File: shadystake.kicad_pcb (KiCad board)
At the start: 2 copper layers, 96.8 x 181.5 mm, 40 parts, among them J1 6P6C, J2 6P6C, J3 6P6C, J4 6P6C, J5 6P6C, J6 6P6C, J7 8P8C

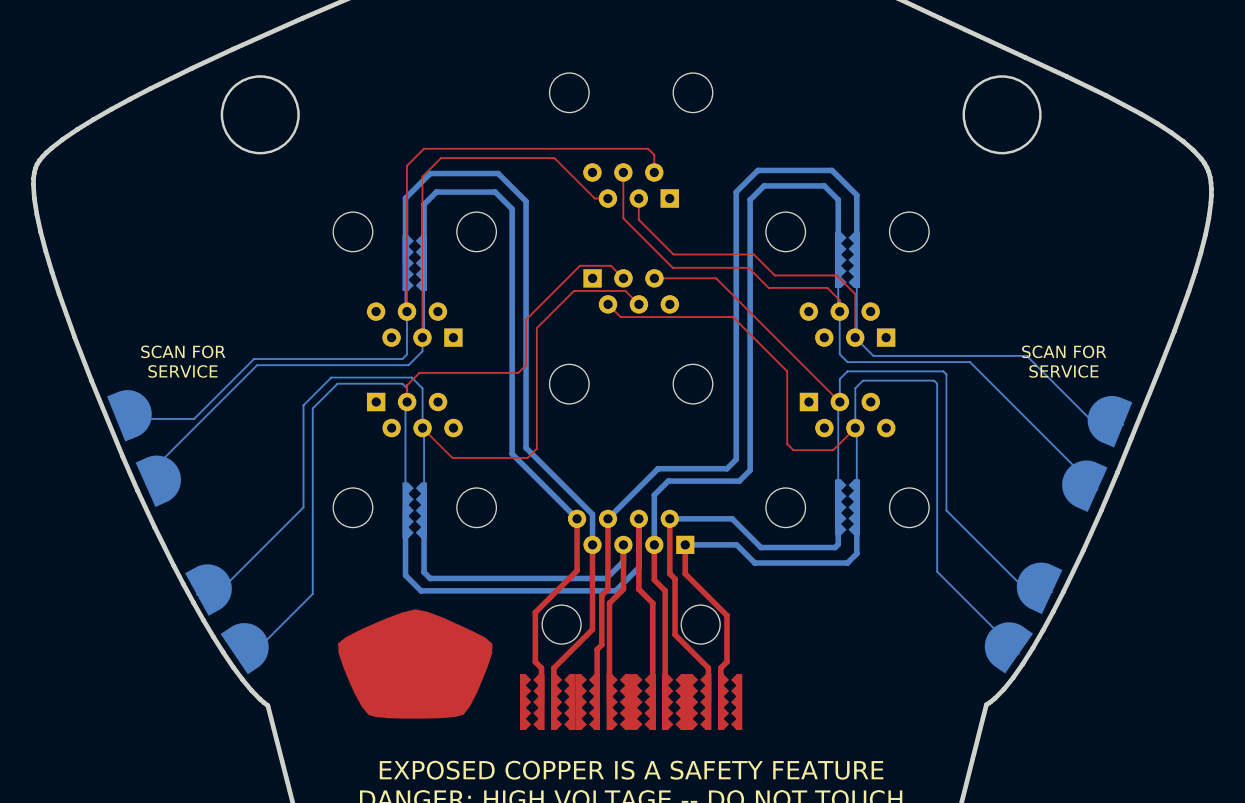
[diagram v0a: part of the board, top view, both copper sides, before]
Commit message: Update to KiCAD 10 and remove circuit protection
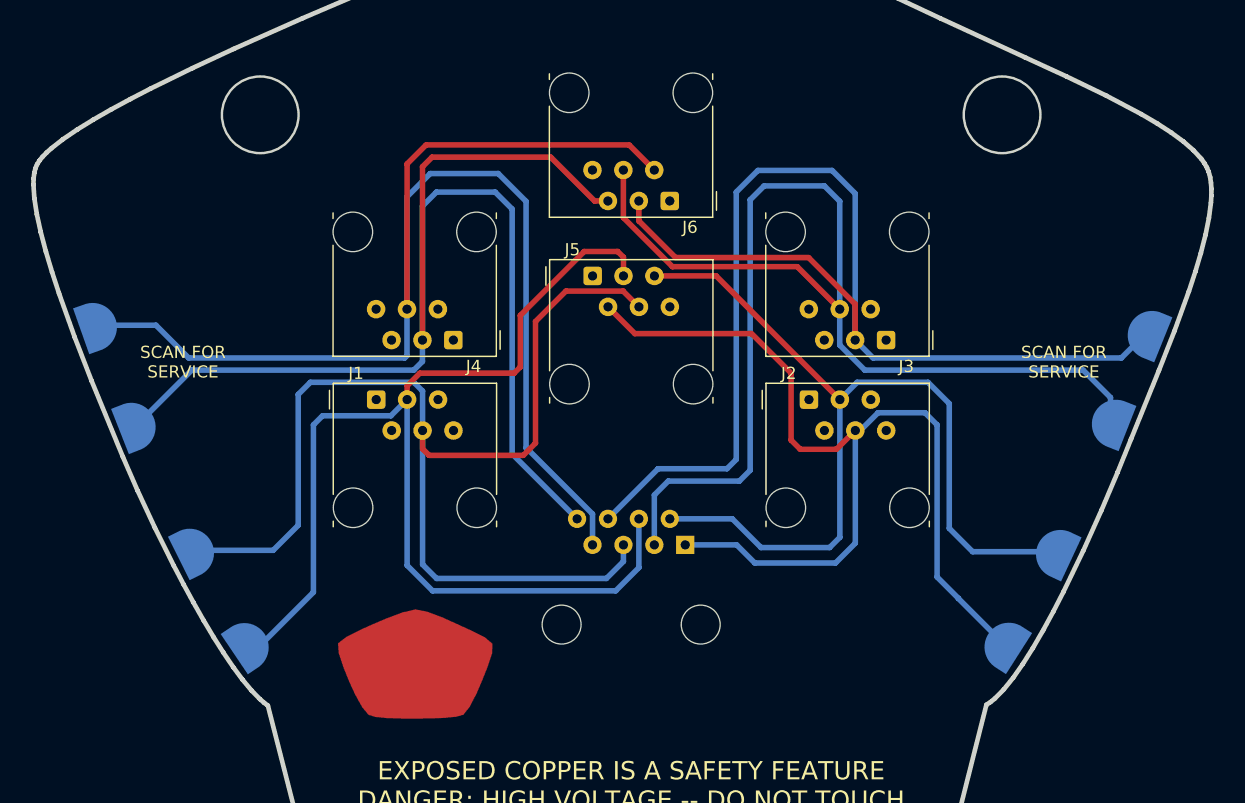
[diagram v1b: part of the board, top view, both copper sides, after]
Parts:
- removed E1, E10, E11, E12, E2, E3, E4, E5, E6, E7, E8, E9: SPARK_GAP, Shadystake:Spark_Gap_Teeth
- J1, J2, J3, J4, J5, J6: footprint Shadystake:6P4C_Vert -> Connector_RJ:RJ12_Amphenol_54601-x06_Horizontal
- moved TP7 7.76 mm to (41.2, 50.8), turned to -160.5 degrees
- moved TP6 7.72 mm to (130.1, 51.5)
- moved TP5 5.60 mm to (127.1, 58.8), turned to -21.5 degrees
- moved TP8 4.85 mm to (44.4, 59.0), turned to -158.5 degrees
- moved TP1 3.31 mm to (49.2, 69.5), turned to -153.5 degrees
- moved TP4 3.11 mm to (122.5, 69.6)
- moved svg2mod 0.20 mm to (43.9, 38.6)
- turned TP3 to -32.5 degrees
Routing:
- net /TIP2: track 104.8 -> 81.7 mm
- net /RING2: track 96.2 -> 76.3 mm
- net /RING1: track 112.3 -> 95.6 mm
- net /RING3: track 123.8 -> 108.6 mm
- net /RING4: track 122.2 -> 107.3 mm
- net /TIP4: track 128.8 -> 115.6 mm
- net /TIP1: track 109.0 -> 95.8 mm
- net /TIP3: track 120.3 -> 109.4 mm

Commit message: Update QR code?
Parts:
- J1, J2, J3, J4, J5, J6: footprint Connector_RJ:RJ12_Amphenol_54601-x06_Horizontal -> Shadystake:RJ12_Amphenol_54601-x06_Horizontal
- svg2mod (x2): footprint Shadystake:fap -> Shadystake:Steak_QR
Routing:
- net /TIP3: track 109.4 -> 108.2 mm

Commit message: Reimport edge.cuts... jfc...
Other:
- outline, holes or cut-outs redrawn

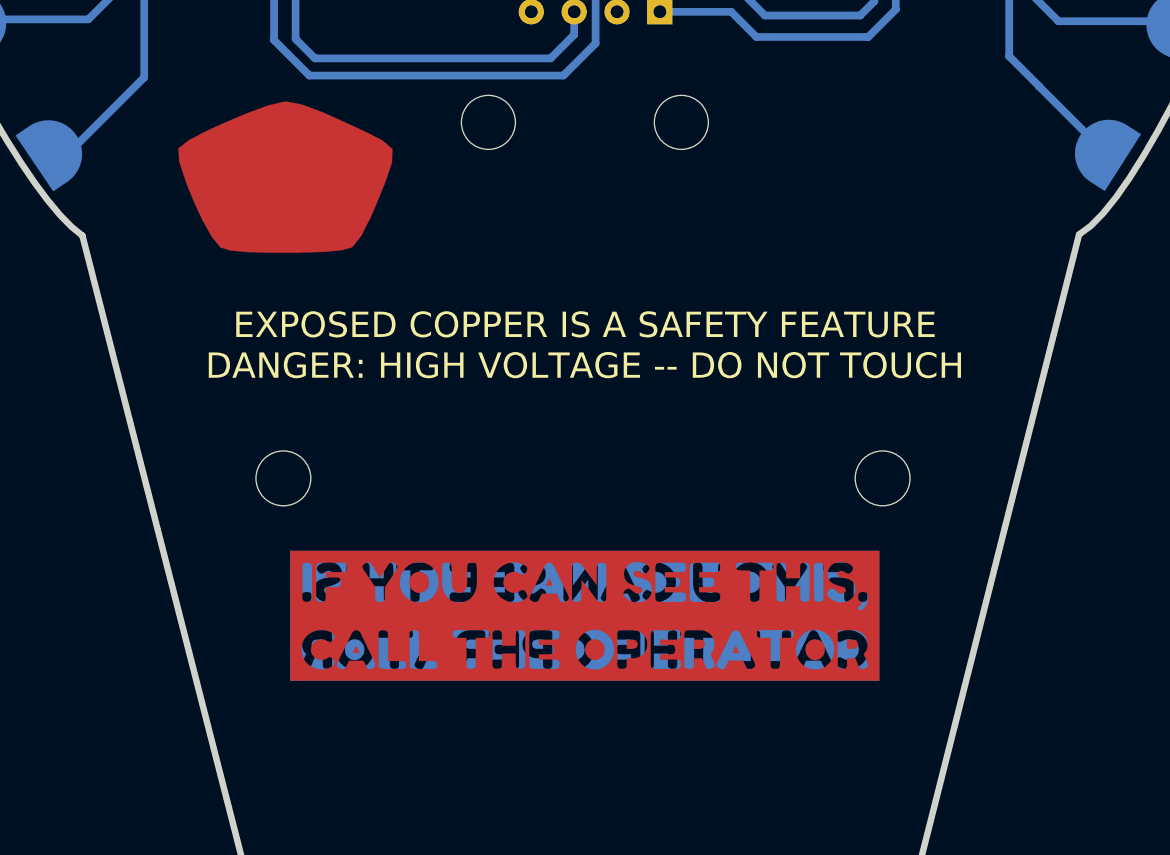
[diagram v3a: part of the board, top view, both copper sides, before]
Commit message: Add silkscreen barcode area and RJ45 eject hole
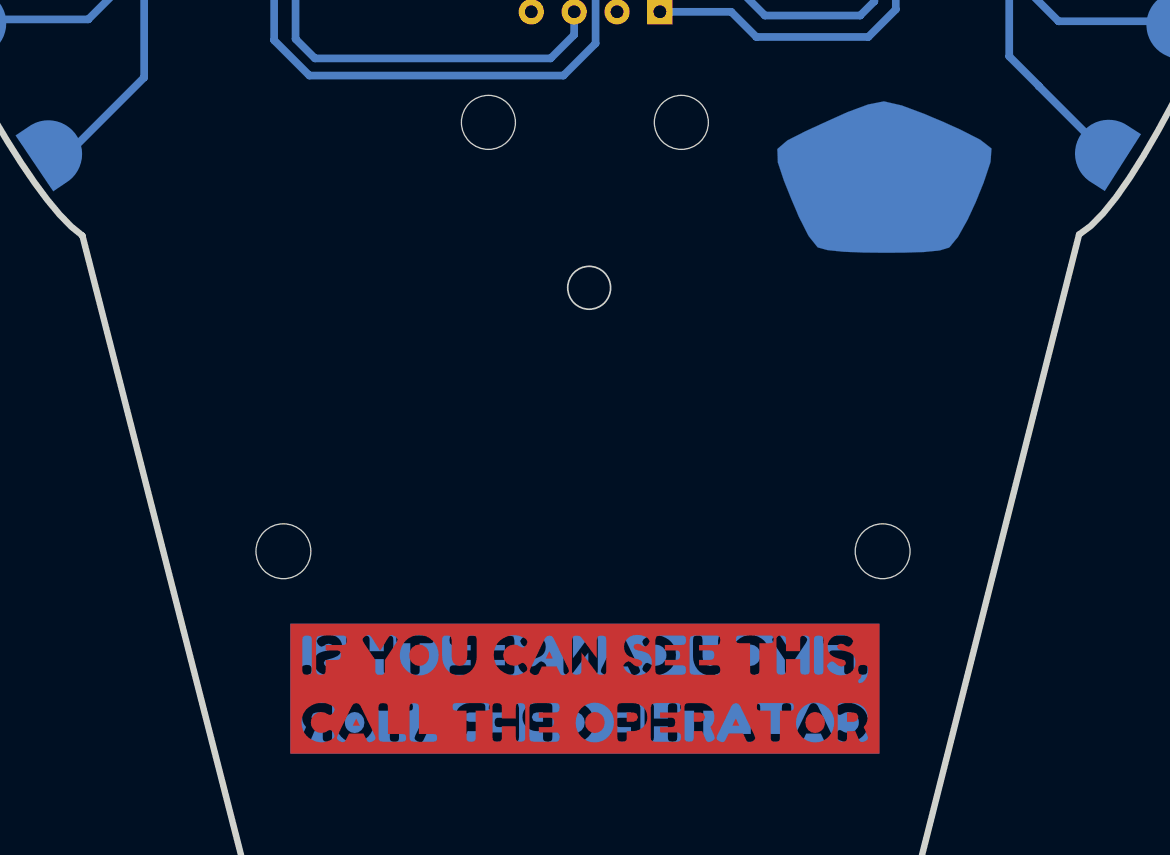
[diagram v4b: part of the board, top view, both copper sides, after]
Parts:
- kibuzzard-62B55316, svg2mod: moved to B.Cu
- svg2mod: moved to F.Cu
- moved svg2mod 53.3 mm to (59.6, 82.4), turned to 0 degrees
- moved svg2mod 48.3 mm to (110.5, 73.7), turned to 180 degrees
- moved kibuzzard-62B55316 36.5 mm to (67.6, 81.3), turned to 180 degrees
- moved ? 4.32 mm to (104.0, 100.3)
- moved ? 4.32 mm to (68.5, 100.3)
- moved kibuzzard-62B55205 4.32 mm to (86.4, 108.5) (x2)
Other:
- outline, holes or cut-outs redrawn
- board text removed: "EXPOSED COPPER IS A SAFETY FEATURE DANGER: HIGH VOLTAGE -- DO NOT TOUCH"

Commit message: Add 2D barcode region
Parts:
- removed kibuzzard-62B55316: G***, kibuzzard-62B55316
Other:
- board text removed: "** PCB ORDER NUM **"

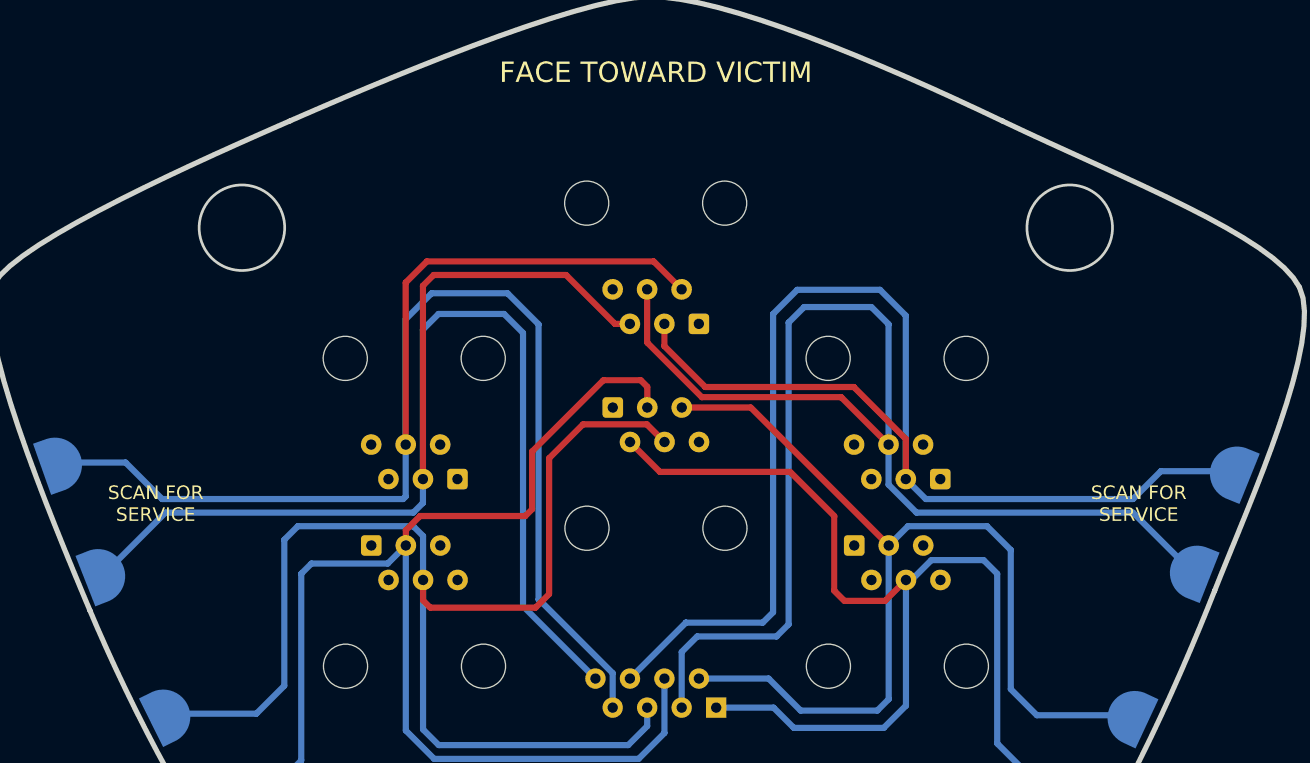
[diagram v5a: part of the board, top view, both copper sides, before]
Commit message: Add enclosure holes
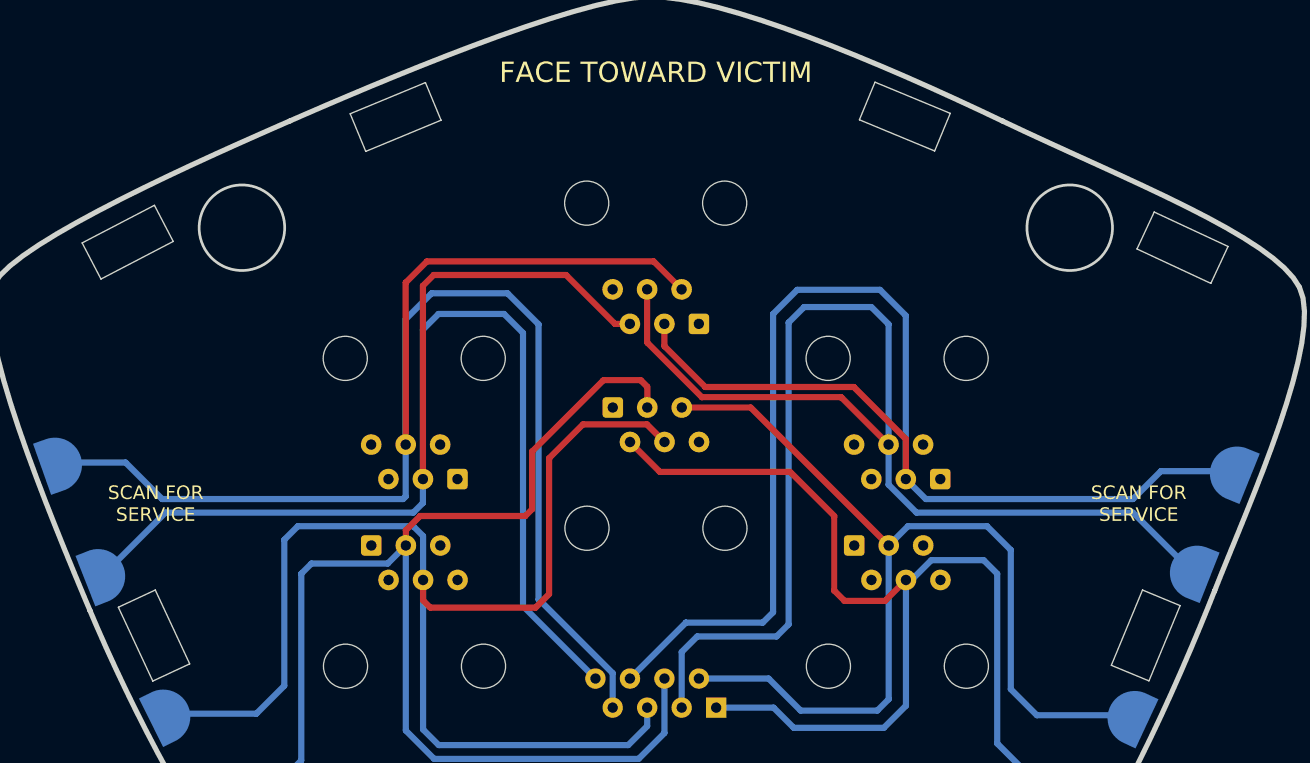
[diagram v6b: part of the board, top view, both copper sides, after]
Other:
- outline, holes or cut-outs redrawn
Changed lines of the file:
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@@
 		(layer "B.SilkS")
+	)
+	(gr_poly
+		(pts
+			(xy 44.114751 34.138965) (xy 49.436816 31.368476) (xy 50.822065 34.029507) (xy 45.5 36.8)
+		)
+		(stroke
+			(width 0.1)
+			(type default)
+		)
+		(fill no)
+		(layer "Edge.Cuts")
+	)
+	(gr_poly
+		(pts
+			(xy 63.851947 24.628359) (xy 69.395224 22.332261) (xy 70.543278 25.103898) (xy 65 27.4)
+		)
+		(stroke
+			(width 0.1)
+			(type default)
+		)
+		(fill no)
+		(layer "Edge.Cuts")
+	)
+	(gr_poly
+		(pts
+			(xy 102.5 22.3) (xy 108.043275 24.596104) (xy 106.895229 27.367746) (xy 101.351951 25.071644)
+		)
+		(stroke
+			(width 0.1)
+			(type default)
+		)
+		(fill no)
+		(layer "Edge.Cuts")
+	)
+	(gr_poly
+		(pts
+			(xy 124.971641 60.848053) (xy 122.675545 66.391327) (xy 119.903903 65.243276) (xy 122.2 59.7)
+		)
+		(stroke
+			(width 0.1)
+			(type default)
+		)
+		(fill no)
+		(layer "Edge.Cuts")
+	)
+	(gr_poly
+		(pts
+			(xy 127.232143 37.118926) (xy 121.794297 34.583219) (xy 123.062152 31.864293) (xy 128.5 34.4)
+		)
+		(stroke
+			(width 0.1)
+			(type default)
+		)
+		(fill no)
+		(layer "Edge.Cuts")
+	)
+	(gr_poly
+		(pts
+			(xy 49.316786 66.405702) (xy 46.781077 60.967857) (xy 49.5 59.7) (xy 52.035712 65.137846)
+		)
+		(stroke
+			(width 0.1)
+			(type default)
+		)
+		(fill no)
+		(layer "Edge.Cuts")
 	)
 	(gr_curve
@@
 			(keep_text_aligned yes)
 		)
-		(gr_text "2.4000 in"
+		(gr_text "60.9600 mm"
 			(at 86.36 31.22 0)
 			(layer "Cmts.User")

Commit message: Add port numbers
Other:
- board text added: "1"
- board text added: "2"
- board text added: "3"
- board text added: "4"
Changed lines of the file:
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@@
 			(plotpadnumbers no)
 			(hidednponfab no)
-			(sketchdnponfab yes)
-			(crossoutdnponfab yes)
+			(sketchdnponfab no)
+			(crossoutdnponfab no)
 			(subtractmaskfromsilk yes)
 			(outputformat 1)
@@
 		(layer "Edge.Cuts")
 	)
+	(gr_text "4"
+		(at 58.928 48.26 0)
+		(layer "F.Mask")
+		(effects
+			(font
+				(size 3 3)
+				(thickness 0.3)
+			)
+			(justify bottom)
+		)
+	)
+	(gr_text "1"
+		(at 58.928 63.5 0)
+		(layer "F.Mask")
+		(effects
+			(font
+				(size 3 3)
+				(thickness 0.3)
+			)
+			(justify bottom)
+		)
+	)
+	(gr_text "3"
+		(at 113.792 48.26 0)
+		(layer "F.Mask")
+		(effects
+			(font
+				(size 3 3)
+				(thickness 0.3)
+			)
+			(justify bottom)
+		)
+	)
+	(gr_text "2\n"
+		(at 113.792 63.5 0)
+		(layer "F.Mask")
+		(effects
+			(font
+				(size 3 3)
+				(thickness 0.3)
+			)
+			(justify bottom)
+		)
+	)
 	(gr_text "SCAN FOR\nSERVICE"
